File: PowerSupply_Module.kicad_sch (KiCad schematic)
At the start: 1 part, among them U12 MP2637AGR-P

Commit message: added power layout
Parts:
- added C39, C43: 100nF, symbol Device:C
- added C40, C41, C42, C45: 120pF, symbol Device:C
- added C44: 47uF, symbol Device:C
- added D10, D11, D9: LED, symbol Device:LED
- added J6: Conn_01x02_Socket, symbol Connector:Conn_01x02_Socket
- added L5: 2.2uH, symbol Device:L
- added R21, R22, R23, R33: 4K7, symbol Device:R
- added R24: R17, symbol Device:R
- added R25: 20k, symbol Device:R
- added R26: 120k, symbol Device:R
- added R27: 33k, symbol Device:R
- added R28, R38, R39: 10k, symbol Device:R
- added R32: 100k, symbol Device:R
- added R34: 75k, symbol Device:R
- added R35: 15k, symbol Device:R
- added R36: 68k, symbol Device:R
- added R37: 22k, symbol Device:R
- added R40: 0R02, symbol Device:R
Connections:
- net GND: now reaches U12.1 (PGND), U12.23 (PGND), U12.24 (PGND)
- net GND: now also U12.6 (AGND), C39.2, C41.2, C42.2, C43.2, C44.2, C45.2, J6.1 (Pin_1), R24.2, R25.2, R26.2, R28.2, R32.2, R35.2, R37.2, R39.2
- net FB: now reaches U12.10 (FB)
- net FB: now also C40.2, R27.2, R28.1
- net at U12.11 (~{ACOK}): now also D10.1 (K)
- net at U12.12 (REG): now also R36.2, R37.1
- net at U12.13 (TMR): now also C43.1
- net at U12.14 (PWIN): now also R34.2, R35.1
- net at U12.15 (ILIM): now also R25.1
- net PUS_VCC: now reaches U12.16 (VCC)
- net PUS_VCC: now also U12.20 (VIN), C39.1, R21.1, R22.1, R23.1, R33.1, R34.1, R36.1
- net BType: now reaches U12.17 (VB)
- net BType: now also R24.1
- net at U12.18 (EN): now also U12.19 (MODE), R33.2
- net at U12.2 (~{CHG}): now also D9.1 (K)
- net +5V: now reaches U12.21 (SYS)
- net +5V: now also C40.1, C41.1, C42.1, C45.1, R27.1, R38.1
- net at U12.22 (SW): now also L5.1
- net at U12.3 (~{BOOST}): now also D11.1 (K)
- net at U12.4 (CSP): now also L5.2, R40.1
- net +BATT: now reaches U12.5 (BATT)
- net +BATT: now also C44.1, J6.2 (Pin_2), R40.2
- net at U12.7 (OLIM): now also R32.1
- net at U12.8 (ISET): now also R26.1
- net NTC: now reaches U12.9 (NTC)
- net NTC: now also R38.2, R39.1
- new net: D9.2 (A), R21.2
- new net: D11.2 (A), R23.2
- new net: D10.2 (A), R22.2
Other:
- note added: "Connector"
- note added: "USV Battery manager"
- note removed: "ChargeManager"
- moved on the sheet: U12

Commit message: added step down
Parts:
- added C46: 100nF, symbol Device:C
- added C47, C48: 470pF, symbol Device:C
- added D12: 1N5819, Diode_THT:D_DO-41_SOD81_P10.16mm_Horizontal, symbol Diode:1N5819
- added J7: Conn_01x02_Socket, symbol Connector:Conn_01x02_Socket
- added L6: 22uH, symbol Device:L_Iron
- added R29: 0.33R, symbol Device:R
- added R30: 3.5k, symbol Device:R
- added R31: 1.2k, symbol Device:R
- added U13: MC34063AD, Package_SO:SOIC-8_3.9x4.9mm_P1.27mm, symbol Regulator_Switching:MC34063AD
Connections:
- net GND: now also C46.2, C47.2, C48.2, D12.2 (A), J7.1 (Pin_1), R31.1, U13.4 (GND)
- net NTC: now also J7.2 (Pin_2)
- net PUS_VCC: no longer U12.20 (VIN)
- new net: D12.1 (K), L6.1, U13.2 (SwE)
- new net: R29.1, U13.1 (SwC), U13.7 (Ipk), U13.8 (DC)
- new net: C47.1, U13.3 (TC)
- new net: R30.1, R31.2, U13.5 (Vfb)
- new net PW+: C46.1, R29.2, U13.6 (Vin)
- new net StpDow_Out: C48.1, L6.2, R30.2, U12.20 (VIN)
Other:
- note added: "Step Down"
- moved on the sheet: C39, C40, C41, C42, C43, C44, C45, D10, D11, D9, J6, L5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

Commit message: done most of the schematics
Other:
- note added: "TODO"
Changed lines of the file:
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@@
 	(wire
 		(pts
-			(xy 66.04 31.75) (xy 71.12 31.75)
-		)
-		(stroke
-			(width 0)
-			(type default)
-		)
-	)
-	(wire
-		(pts
 			(xy 123.19 96.52) (xy 123.19 93.98)
 		)
@@
 	(wire
 		(pts
-			(xy 64.77 31.75) (xy 66.04 31.75)
+			(xy 66.04 31.75) (xy 64.77 31.75)
 		)
 		(stroke
@@
 	(wire
 		(pts
-			(xy 199.39 100.33) (xy 208.28 100.33)
+			(xy 199.39 100.33) (xy 204.47 100.33)
 		)
 		(stroke
@@
 	(wire
 		(pts
-			(xy 179.07 101.6) (xy 170.18 101.6)
+			(xy 177.8 101.6) (xy 170.18 101.6)
 		)
 		(stroke
@@
 	(wire
 		(pts
-			(xy 170.18 99.06) (xy 179.07 99.06)
+			(xy 170.18 99.06) (xy 177.8 99.06)
 		)
 		(stroke
@@
 	(wire
 		(pts
-			(xy 208.28 102.87) (xy 199.39 102.87)
+			(xy 204.47 102.87) (xy 199.39 102.87)
 		)
 		(stroke
@@
 		)
 	)
+	(text "TODO"
+		(exclude_from_sim no)
+		(at 70.866 102.616 0)
+		(effects
+			(font
+				(size 1.27 1.27)
+			)
+		)
+	)
+	(label "NTC"
+		(at 204.47 100.33 0)
+		(fields_autoplaced yes)
+		(effects
+			(font
+				(size 1.27 1.27)
+			)
+			(justify left bottom)
+		)
+	)
 	(label "FB"
 		(at 88.9 86.36 0)
@@
 		)
 	)
-	(global_label "NTC"
-		(shape input)
-		(at 71.12 31.75 0)
-		(fields_autoplaced yes)
-		(effects
-			(font
-				(size 1.27 1.27)
-			)
-			(justify left)
-		)
-		(property "Intersheetrefs" "${INTERSHEET_REFS}"
-			(at 77.6733 31.75 0)
-			(effects
-				(font
-					(size 1.27 1.27)
-				)
-				(justify left)
-				(hide yes)
-			)
-		)
-	)
 	(global_label "PUS_VCC"
 		(shape input)
@@
 		)
 	)
-	(global_label "NTC"
-		(shape input)
-		(at 208.28 100.33 90)
-		(fields_autoplaced yes)
-		(effects
-			(font
-				(size 1.27 1.27)
-			)
-			(justify left)
-		)
-		(property "Intersheetrefs" "${INTERSHEET_REFS}"
-			(at 208.28 93.7767 90)
-			(effects
-				(font
-					(size 1.27 1.27)
-				)
-				(justify left)
-				(hide yes)
-			)
-		)
-	)
 	(global_label "StpDow_Out"
 		(shape input)
@@
 	(symbol
 		(lib_id "power:+BATT")
-		(at 179.07 99.06 0)
+		(at 177.8 99.06 0)
 		(unit 1)
 		(exclude_from_sim no)
@@
 		(dnp no)
 		(property "Reference" "#PWR043"
-			(at 179.07 102.87 0)
+			(at 177.8 102.87 0)
 			(effects
 				(font
@@
 		)
 		(property "Value" "+BATT"
-			(at 179.07 93.98 0)
+			(at 177.8 93.98 0)
 			(effects
 				(font
@@
 		)
 		(property "Footprint" ""
-			(at 179.07 99.06 0)
+			(at 177.8 99.06 0)
 			(effects
 				(font
@@
 		)
 		(property "Datasheet" ""
-			(at 179.07 99.06 0)
+			(at 177.8 99.06 0)
 			(effects
 				(font
@@
 		)
 		(property "Description" "Power symbol creates a global label with name \"+BATT\""
-			(at 179.07 99.06 0)
+			(at 177.8 99.06 0)
 			(effects
 				(font
@@
 		(dnp no)
 		(property "Reference" "J7"
-			(at 194.945 95.25 0)
+			(at 194.31 92.964 0)
 			(effects
 				(font
@@
 		)
 		(property "Value" "Conn_01x02_Socket"
-			(at 194.945 97.79 0)
+			(at 194.31 95.504 0)
 			(effects
 				(font
@@
 		(dnp no)
 		(property "Reference" "J6"
-			(at 165.735 93.98 0)
+			(at 165.1 91.694 0)
 			(effects
 				(font
@@
 		)
 		(property "Value" "Conn_01x02_Socket"
-			(at 165.735 96.52 0)
+			(at 165.1 94.234 0)
 			(effects
 				(font
@@
 	(symbol
 		(lib_id "power:GND")
-		(at 179.07 101.6 0)
+		(at 177.8 101.6 0)
 		(unit 1)
 		(exclude_from_sim no)
@@
 		(fields_autoplaced yes)
 		(property "Reference" "#PWR050"
-			(at 179.07 107.95 0)
+			(at 177.8 107.95 0)
 			(effects
 				(font
@@
 		)
 		(property "Value" "GND"
-			(at 179.07 106.68 0)
+			(at 177.8 106.68 0)
 			(effects
 				(font
@@
 		)
 		(property "Footprint" ""
-			(at 179.07 101.6 0)
+			(at 177.8 101.6 0)
 			(effects
 				(font
@@
 		)
 		(property "Datasheet" ""
-			(at 179.07 101.6 0)
+			(at 177.8 101.6 0)
 			(effects
 				(font
@@
 		)
 		(property "Description" "Power symbol creates a global label with name \"GND\" , ground"
-			(at 179.07 101.6 0)
+			(at 177.8 101.6 0)
 			(effects
 				(font
@@
 	(symbol
 		(lib_id "power:GND")
-		(at 208.28 102.87 0)
+		(at 204.47 102.87 0)
 		(unit 1)
 		(exclude_from_sim no)
@@
 		(fields_autoplaced yes)
 		(property "Reference" "#PWR071"
-			(at 208.28 109.22 0)
+			(at 204.47 109.22 0)
 			(effects
 				(font
@@
 		)
 		(property "Value" "GND"
-			(at 208.28 107.95 0)
+			(at 204.47 107.95 0)
 			(effects
 				(font
@@
 		)
 		(property "Footprint" ""
-			(at 208.28 102.87 0)
+			(at 204.47 102.87 0)
 			(effects
 				(font
@@
 		)
 		(property "Datasheet" ""
-			(at 208.28 102.87 0)
+			(at 204.47 102.87 0)
 			(effects
 				(font
@@
 		)
 		(property "Description" "Power symbol creates a global label with name \"GND\" , ground"
-			(at 208.28 102.87 0)
+			(at 204.47 102.87 0)
 			(effects
 				(font

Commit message: done refacoring
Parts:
- D10, D11, D9: footprint (none) -> Capacitor_SMD:C_0603_1608Metric
- J6, J7: footprint (none) -> Connector_PinHeader_1.00mm:PinHeader_1x02_P1.00mm_Vertical
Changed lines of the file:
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@@
 			)
 		)
-		(property "Footprint" ""
+		(property "Footprint" "Capacitor_SMD:C_0603_1608Metric"
 			(at 113.03 90.17 0)
 			(effects
@@
 			)
 		)
-		(property "Footprint" ""
+		(property "Footprint" "Capacitor_SMD:C_0603_1608Metric"
 			(at 133.35 90.17 0)
 			(effects
@@
 			)
 		)
-		(property "Footprint" ""
+		(property "Footprint" "Connector_PinHeader_1.00mm:PinHeader_1x02_P1.00mm_Vertical"
 			(at 194.31 102.87 0)
 			(effects
@@
 			)
 		)
-		(property "Footprint" ""
+		(property "Footprint" "Connector_PinHeader_1.00mm:PinHeader_1x02_P1.00mm_Vertical"
 			(at 165.1 101.6 0)
 			(effects
@@
 			)
 		)
-		(property "Footprint" ""
+		(property "Footprint" "Capacitor_SMD:C_0603_1608Metric"
 			(at 123.19 90.17 0)
 			(effects

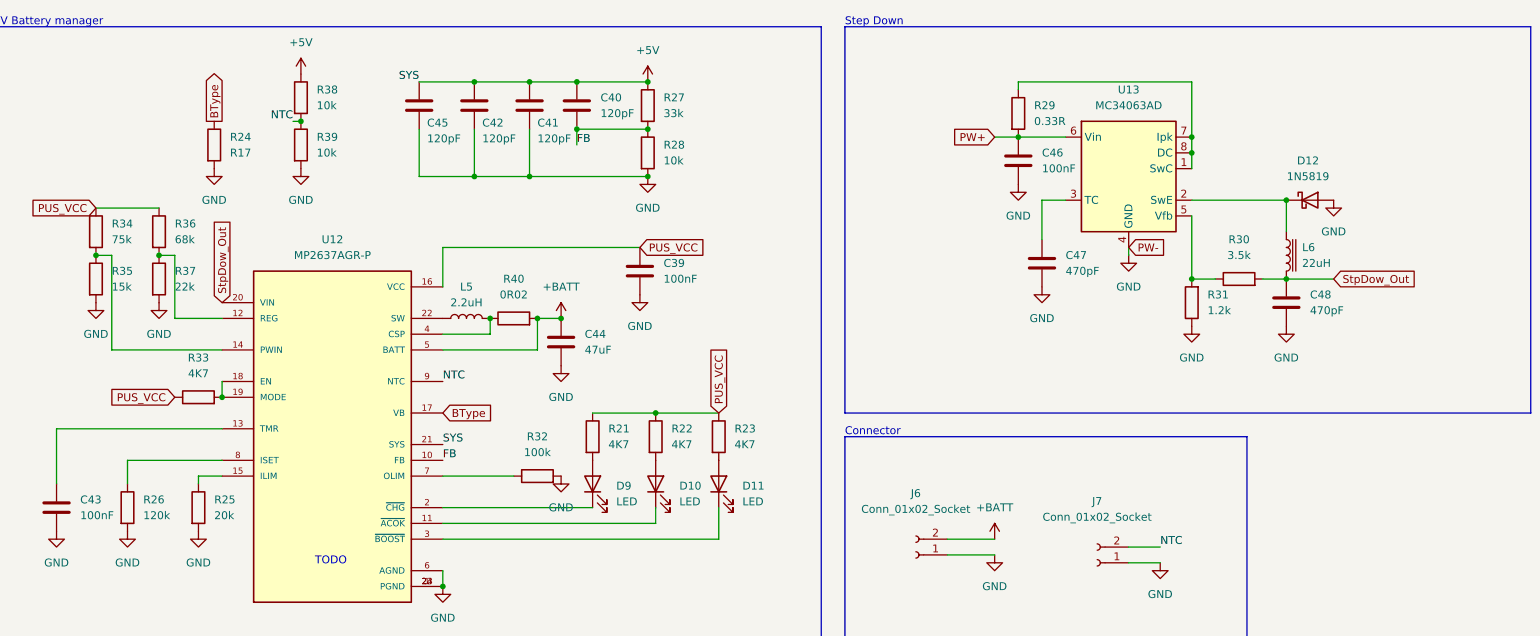
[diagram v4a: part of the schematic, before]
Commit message: assigned most footprints
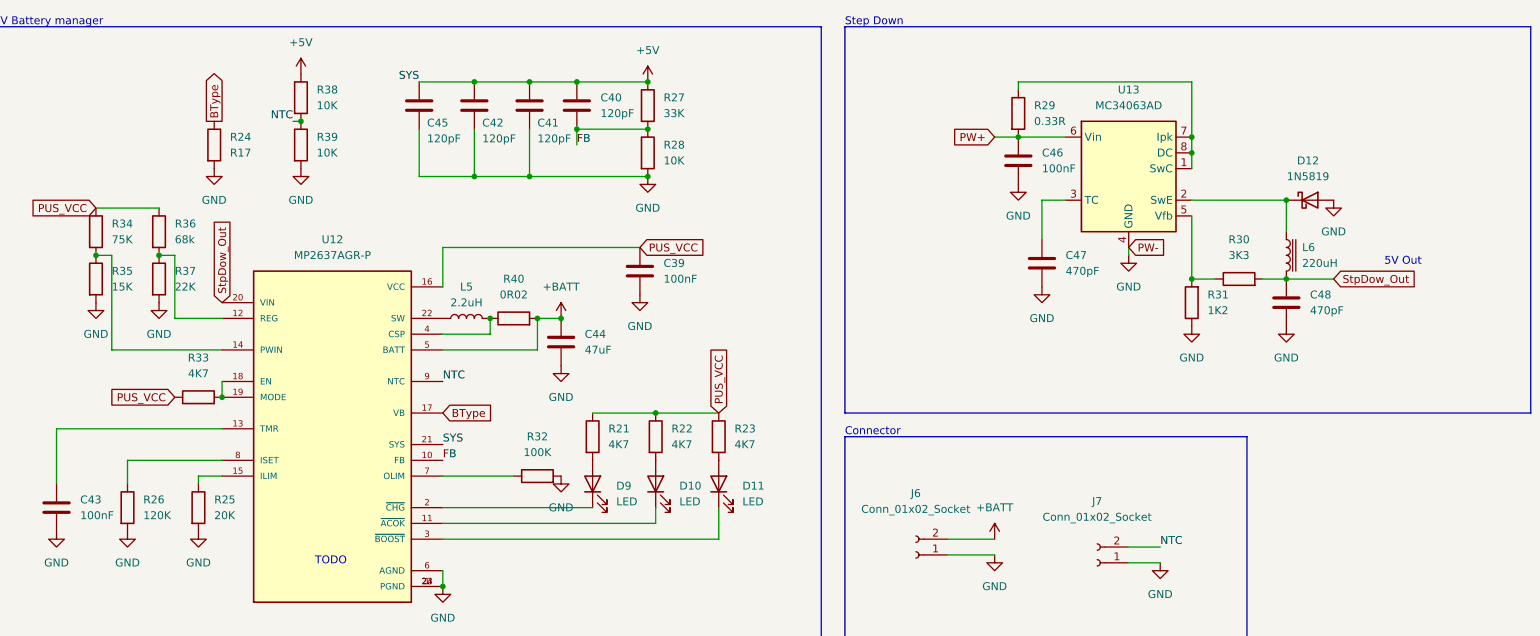
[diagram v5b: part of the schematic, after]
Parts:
- L5: footprint (none) -> Inductor_SMD:L_Bourns_SRP7028A_7.3x6.6mm
- L6: value 22uH -> 220uH; footprint (none) -> Inductor_SMD:L_7.3x7.3_H4.5
- R21, R22, R23, R24, R29, R33, R36, R40: footprint (none) -> Resistor_SMD:R_0603_1608Metric
- R25: value 20k -> 20K; footprint (none) -> Resistor_SMD:R_0603_1608Metric
- R26: value 120k -> 120K; footprint (none) -> Resistor_SMD:R_0603_1608Metric
- R27: value 33k -> 33K; footprint (none) -> Resistor_SMD:R_0603_1608Metric
- R28, R38, R39: value 10k -> 10K; footprint (none) -> Resistor_SMD:R_0603_1608Metric
- R30: value 3.5k -> 3K3; footprint (none) -> Resistor_SMD:R_0603_1608Metric
- R31: value 1.2k -> 1K2; footprint (none) -> Resistor_SMD:R_0603_1608Metric
- R32: value 100k -> 100K; footprint (none) -> Resistor_SMD:R_0603_1608Metric
- R34: value 75k -> 75K; footprint (none) -> Resistor_SMD:R_0603_1608Metric
- R35: value 15k -> 15K; footprint (none) -> Resistor_SMD:R_0603_1608Metric
- R37: value 22k -> 22K; footprint (none) -> Resistor_SMD:R_0603_1608Metric
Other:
- note added: "5V Out"
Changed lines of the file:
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@@
 		)
 	)
+	(text "5V Out"
+		(exclude_from_sim no)
+		(at 243.586 54.356 0)
+		(effects
+			(font
+				(size 1.27 1.27)
+			)
+		)
+	)
 	(text "Step Down"
 		(exclude_from_sim no)
@@
 			)
 		)
-		(property "Footprint" ""
+		(property "Footprint" "Resistor_SMD:R_0603_1608Metric"
 			(at 100.33 65.278 90)
 			(effects
@@
 			)
 		)
-		(property "Footprint" ""
+		(property "Footprint" "Resistor_SMD:R_0603_1608Metric"
 			(at 111.252 82.55 90)
 			(effects
@@
 			)
 		)
-		(property "Footprint" ""
+		(property "Footprint" "Inductor_SMD:L_Bourns_SRP7028A_7.3x6.6mm"
 			(at 92.71 63.5 0)
 			(effects
@@
 			)
 		)
-		(property "Value" "15k"
+		(property "Value" "15K"
 			(at 35.56 58.4199 0)
 			(effects
@@
 			)
 		)
-		(property "Footprint" ""
+		(property "Footprint" "Resistor_SMD:R_0603_1608Metric"
 			(at 31.242 57.15 90)
 			(effects
@@
 			)
 		)
-		(property "Value" "10k"
+		(property "Value" "10K"
 			(at 68.58 36.8299 0)
 			(effects
@@
 			)
 		)
-		(property "Footprint" ""
+		(property "Footprint" "Resistor_SMD:R_0603_1608Metric"
 			(at 64.262 35.56 90)
 			(effects
@@
 			)
 		)
-		(property "Value" "10k"
+		(property "Value" "10K"
 			(at 68.58 29.2099 0)
 			(effects
@@
 			)
 		)
-		(property "Footprint" ""
+		(property "Footprint" "Resistor_SMD:R_0603_1608Metric"
 			(at 64.262 27.94 90)
 			(effects
@@
 			)
 		)
-		(property "Footprint" ""
+		(property "Footprint" "Resistor_SMD:R_0603_1608Metric"
 			(at 41.402 49.53 90)
 			(effects
@@
 			)
 		)
-		(property "Value" "75k"
+		(property "Value" "75K"
 			(at 35.56 50.7999 0)
 			(effects
@@
 			)
 		)
-		(property "Footprint" ""
+		(property "Footprint" "Resistor_SMD:R_0603_1608Metric"
 			(at 31.242 49.53 90)
 			(effects
@@
 			)
 		)
-		(property "Footprint" ""
+		(property "Footprint" "Resistor_SMD:R_0603_1608Metric"
 			(at 131.572 82.55 90)
 			(effects
@@
 			)
 		)
-		(property "Value" "20k"
+		(property "Value" "20K"
 			(at 52.07 95.2499 0)
 			(effects
@@
 			)
 		)
-		(property "Footprint" ""
+		(property "Footprint" "Resistor_SMD:R_0603_1608Metric"
 			(at 47.752 93.98 90)
 			(effects
@@
 			)
 		)
-		(property "Value" "33k"
+		(property "Value" "33K"
 			(at 124.46 30.4799 0)
 			(effects
@@
 			)
 		)
-		(property "Footprint" ""
+		(property "Footprint" "Resistor_SMD:R_0603_1608Metric"
 			(at 120.142 29.21 90)
 			(effects
@@
 			)
 		)
-		(property "Value" "120k"
+		(property "Value" "120K"
 			(at 40.64 95.2499 0)
 			(effects
@@
 			)
 		)
-		(property "Footprint" ""
+		(property "Footprint" "Resistor_SMD:R_0603_1608Metric"
 			(at 36.322 93.98 90)
 			(effects
@@
 			)
 		)
-		(property "Footprint" ""
+		(property "Footprint" "Resistor_SMD:R_0603_1608Metric"
 			(at 121.412 82.55 90)
 			(effects
@@
 			)
 		)
-		(property "Footprint" ""
+		(property "Footprint" "Resistor_SMD:R_0603_1608Metric"
 			(at 50.292 35.56 90)
 			(effects
@@
 			)
 		)
-		(property "Value" "10k"
+		(property "Value" "10K"
 			(at 124.46 38.0999 0)
 			(effects
@@
 			)
 		)
-		(property "Footprint" ""
+		(property "Footprint" "Resistor_SMD:R_0603_1608Metric"
 			(at 120.142 36.83 90)
 			(effects
@@
 			)
 		)
-		(property "Value" "100k"
+		(property "Value" "100K"
 			(at 104.14 85.09 90)
 			(effects
@@
 			)
 		)
-		(property "Footprint" ""
+		(property "Footprint" "Resistor_SMD:R_0603_1608Metric"
 			(at 104.14 90.678 90)
 			(effects
@@
 			)
 		)
-		(property "Value" "22uH"
+		(property "Value" "220uH"
 			(at 227.33 54.6099 0)
 			(effects
@@
 			)
 		)
-		(property "Footprint" ""
+		(property "Footprint" "Inductor_SMD:L_7.3x7.3_H4.5"
 			(at 224.79 53.34 0)
 			(effects
@@
 			)
 		)
-		(property "Footprint" ""
+		(property "Footprint" "Resistor_SMD:R_0603_1608Metric"
 			(at 179.832 30.48 90)
 			(effects
@@
 			)
 		)
-		(property "Footprint" ""
+		(property "Footprint" "Resistor_SMD:R_0603_1608Metric"
 			(at 49.53 77.978 90)
 			(effects
@@
 			)
 		)
-		(property "Value" "3.5k"
+		(property "Value" "3K3"
 			(at 217.17 53.34 90)
 			(effects
@@
 			)
 		)
-		(property "Footprint" ""
+		(property "Footprint" "Resistor_SMD:R_0603_1608Metric"
 			(at 217.17 58.928 90)
 			(effects
@@
 			)
 		)
-		(property "Value" "22k"
+		(property "Value" "22K"
 			(at 45.72 58.4199 0)
 			(effects
@@
 			)
 		)
-		(property "Footprint" ""
+		(property "Footprint" "Resistor_SMD:R_0603_1608Metric"
 			(at 41.402 57.15 90)
 			(effects
@@
 			)
 		)
-		(property "Value" "1.2k"
+		(property "Value" "1K2"
 			(at 212.09 62.2299 0)
 			(effects
@@
 			)
 		)
-		(property "Footprint" ""
+		(property "Footprint" "Resistor_SMD:R_0603_1608Metric"
 			(at 211.328 60.96 90)
 			(effects
